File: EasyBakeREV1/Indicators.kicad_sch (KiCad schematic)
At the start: 15 parts, among them U10 STP08CP05

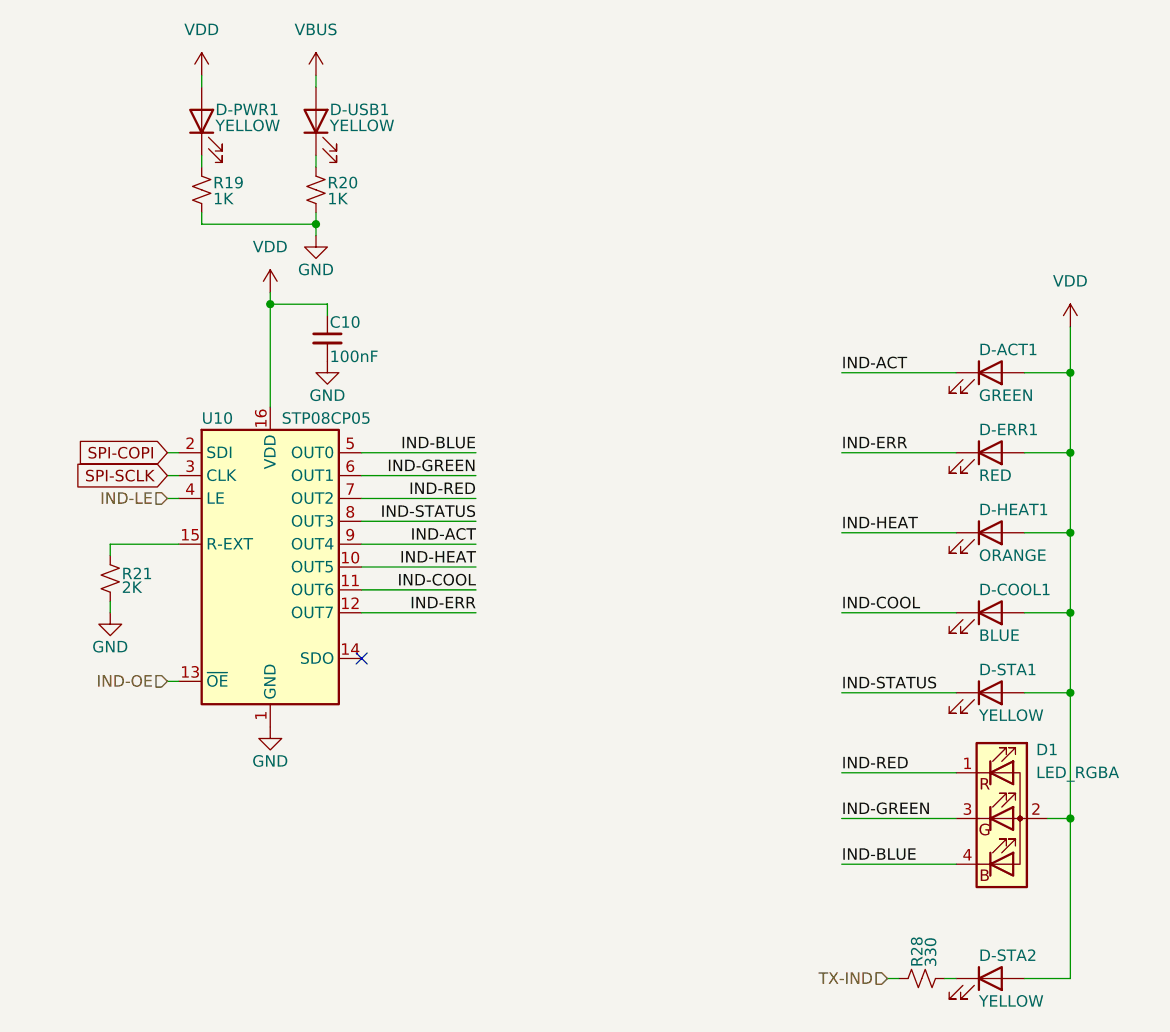
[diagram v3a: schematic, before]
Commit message: Change main pwr to 3.3 due to USB issues
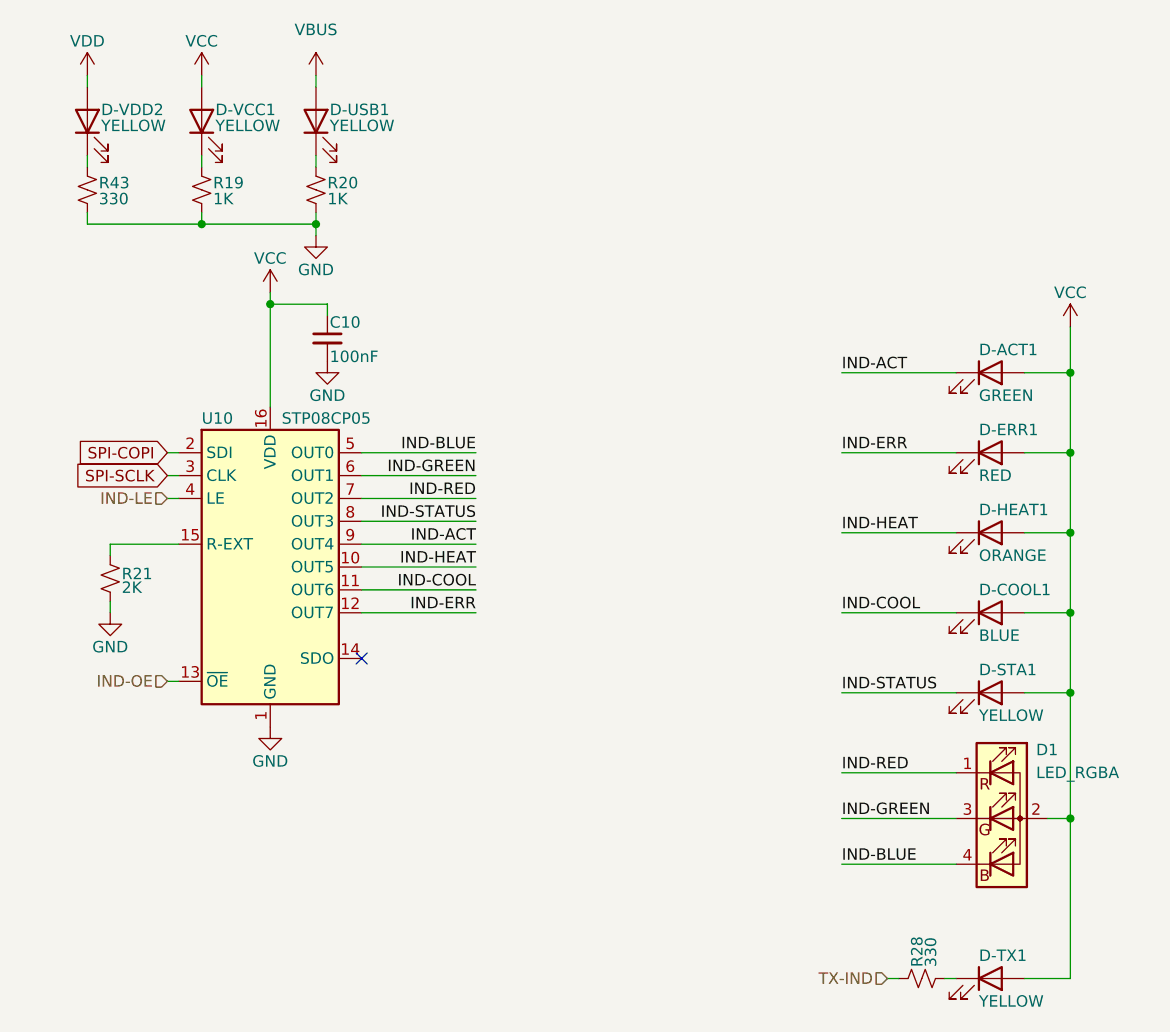
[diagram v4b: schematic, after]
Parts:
- added D-VDD2: YELLOW, LED_SMD:LED_0805_2012Metric_Pad1.15x1.40mm_HandSolder, symbol Device:LED
- added R43: 330, Resistor_SMD:R_0805_2012Metric, symbol Device:R_Small_US
- renumbered D-STA2 to D-TX1, D-PWR1 to D-VCC1
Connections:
- net GND: now also R43.2
- net VDD: now also D-VDD2.2 (A); no longer C10.1, D-ACT1.2 (A), D-COOL1.2 (A), D-ERR1.2 (A), D-HEAT1.2 (A), D-STA1.2 (A), D-TX1.2 (A), D-VCC1.2 (A), D1.2 (GK), U10.16 (VDD)
- new net: D-VDD2.1 (K), R43.1
- new net VCC: C10.1, D-ACT1.2 (A), D-COOL1.2 (A), D-ERR1.2 (A), D-HEAT1.2 (A), D-STA1.2 (A), D-TX1.2 (A), D-VCC1.2 (A), D1.2 (GK), U10.16 (VDD)
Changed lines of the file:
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@@
   (junction (at 45.72 50.8) (diameter 0) (color 0 0 0 0)
+  )
+  (junction (at 38.1 41.91) (diameter 0) (color 0 0 0 0)
   )
   (junction (at 134.62 85.09) (diameter 0) (color 0 0 0 0)
@@
     (stroke (width 0) (type default))
   )
+  (wire (pts (xy 25.4 41.91) (xy 38.1 41.91))
+    (stroke (width 0) (type default))
+  )
   (wire (pts (xy 129.54 67.31) (xy 134.62 67.31))
     (stroke (width 0) (type default))
@@
     (stroke (width 0) (type default))
   )
+  (wire (pts (xy 25.4 40.64) (xy 25.4 41.91))
+    (stroke (width 0) (type default))
+  )
   (wire (pts (xy 109.22 113.03) (xy 121.92 113.03))
     (stroke (width 0) (type default))
@@
     (stroke (width 0) (type default))
   )
+  (wire (pts (xy 25.4 25.4) (xy 25.4 26.67))
+    (stroke (width 0) (type default))
+  )
   (wire (pts (xy 114.3 125.73) (xy 115.57 125.73))
     (stroke (width 0) (type default))
@@
   )
   (wire (pts (xy 34.29 92.71) (xy 35.56 92.71))
+    (stroke (width 0) (type default))
+  )
+  (wire (pts (xy 25.4 34.29) (xy 25.4 35.56))
     (stroke (width 0) (type default))
   )
@@
     )
   )
-  (symbol (lib_id "power:VDD") (at 134.62 53.34 0) (unit 1)
-    (in_bom yes) (on_board yes) (dnp no) (fields_autoplaced)
-    (property "Reference" "#PWR0103" (at 134.62 57.15 0)
-      (effects (font (size 1.27 1.27)) hide)
-    )
-    (property "Value" "VDD" (at 134.62 48.26 0)
-      (effects (font (size 1.27 1.27)))
-    )
-    (property "Footprint" "" (at 134.62 53.34 0)
-      (effects (font (size 1.27 1.27)) hide)
-    )
-    (property "Datasheet" "" (at 134.62 53.34 0)
-      (effects (font (size 1.27 1.27)) hide)
-    )
-    (pin "1")
-    (instances
-      (project "EasyBakeREV1"
-        (path "/e63e39d7-6ac0-4ffd-8aa3-1841a4541b55/a9601474-acad-4e52-ad82-40858ef5b30f"
-          (reference "#PWR0103") (unit 1)
-        )
-      )
-    )
-  )
   (symbol (lib_id "power:GND") (at 50.8 43.18 0) (unit 1)
     (in_bom yes) (on_board yes) (dnp no)
@@
     )
   )
+  (symbol (lib_id "power:VCC") (at 45.72 49.53 0) (unit 1)
+    (in_bom yes) (on_board yes) (dnp no)
+    (property "Reference" "#PWR012" (at 45.72 53.34 0)
+      (effects (font (size 1.27 1.27)) hide)
+    )
+    (property "Value" "VCC" (at 45.72 45.72 0)
+      (effects (font (size 1.27 1.27)))
+    )
+    (property "Footprint" "" (at 45.72 49.53 0)
+      (effects (font (size 1.27 1.27)) hide)
+    )
+    (property "Datasheet" "" (at 45.72 49.53 0)
+      (effects (font (size 1.27 1.27)) hide)
+    )
+    (pin "1")
+    (instances
+      (project "EasyBakeREV1"
+        (path "/e63e39d7-6ac0-4ffd-8aa3-1841a4541b55/a9601474-acad-4e52-ad82-40858ef5b30f"
+          (reference "#PWR012") (unit 1)
+        )
+      )
+    )
+  )
   (symbol (lib_id "Device:LED") (at 38.1 30.48 90) (unit 1)
     (in_bom yes) (on_board yes) (dnp no)
-    (property "Reference" "D-PWR1" (at 39.624 29.21 90)
+    (property "Reference" "D-VCC1" (at 39.624 29.21 90)
       (effects (font (size 1.27 1.27)) (justify right))
     )
@@
       (project "EasyBakeREV1"
         (path "/e63e39d7-6ac0-4ffd-8aa3-1841a4541b55/a9601474-acad-4e52-ad82-40858ef5b30f"
-          (reference "D-PWR1") (unit 1)
+          (reference "D-VCC1") (unit 1)
+        )
+      )
+    )
+  )
+  (symbol (lib_id "power:VCC") (at 134.62 53.34 0) (unit 1)
+    (in_bom yes) (on_board yes) (dnp no)
+    (property "Reference" "#PWR04" (at 134.62 57.15 0)
+      (effects (font (size 1.27 1.27)) hide)
+    )
+    (property "Value" "VCC" (at 134.62 49.53 0)
+      (effects (font (size 1.27 1.27)))
+    )
+    (property "Footprint" "" (at 134.62 53.34 0)
+      (effects (font (size 1.27 1.27)) hide)
+    )
+    (property "Datasheet" "" (at 134.62 53.34 0)
+      (effects (font (size 1.27 1.27)) hide)
+    )
+    (pin "1")
+    (instances
+      (project "EasyBakeREV1"
+        (path "/e63e39d7-6ac0-4ffd-8aa3-1841a4541b55/a9601474-acad-4e52-ad82-40858ef5b30f"
+          (reference "#PWR04") (unit 1)
         )
       )
@@
     )
   )
+  (symbol (lib_id "Device:LED") (at 25.4 30.48 90) (unit 1)
+    (in_bom yes) (on_board yes) (dnp no)
+    (property "Reference" "D-VDD2" (at 26.924 29.21 90)
+      (effects (font (size 1.27 1.27)) (justify right))
+    )
+    (property "Value" "YELLOW" (at 26.924 30.988 90)
+      (effects (font (size 1.27 1.27)) (justify right))
+    )
+    (property "Footprint" "LED_SMD:LED_0805_2012Metric_Pad1.15x1.40mm_HandSolder" (at 25.4 30.48 0)
+      (effects (font (size 1.27 1.27)) hide)
+    )
+    (property "Datasheet" "~" (at 25.4 30.48 0)
+      (effects (font (size 1.27 1.27)) hide)
+    )
+    (pin "1")
+    (pin "2")
+    (instances
+      (project "EasyBakeREV1"
+        (path "/e63e39d7-6ac0-4ffd-8aa3-1841a4541b55/a9601474-acad-4e52-ad82-40858ef5b30f"
+          (reference "D-VDD2") (unit 1)
+        )
+      )
+    )
+  )
   (symbol (lib_id "Device:LED") (at 50.8 30.48 90) (unit 1)
     (in_bom yes) (on_board yes) (dnp no)
@@
   (symbol (lib_id "Device:LED") (at 125.73 125.73 0) (unit 1)
     (in_bom yes) (on_board yes) (dnp no)
-    (property "Reference" "D-STA2" (at 124.46 123.19 0)
+    (property "Reference" "D-TX1" (at 124.46 123.19 0)
       (effects (font (size 1.27 1.27)) (justify left))
     )
@@
       (project "EasyBakeREV1"
         (path "/e63e39d7-6ac0-4ffd-8aa3-1841a4541b55/a9601474-acad-4e52-ad82-40858ef5b30f"
-          (reference "D-STA2") (unit 1)
+          (reference "D-TX1") (unit 1)
         )
       )
@@
     )
   )
-  (symbol (lib_id "power:VDD") (at 45.72 49.53 0) (unit 1)
-    (in_bom yes) (on_board yes) (dnp no) (fields_autoplaced)
-    (property "Reference" "#PWR0105" (at 45.72 53.34 0)
-      (effects (font (size 1.27 1.27)) hide)
-    )
-    (property "Value" "VDD" (at 45.72 44.45 0)
-      (effects (font (size 1.27 1.27)))
-    )
-    (property "Footprint" "" (at 45.72 49.53 0)
-      (effects (font (size 1.27 1.27)) hide)
-    )
-    (property "Datasheet" "" (at 45.72 49.53 0)
-      (effects (font (size 1.27 1.27)) hide)
-    )
-    (pin "1")
-    (instances
-      (project "EasyBakeREV1"
-        (path "/e63e39d7-6ac0-4ffd-8aa3-1841a4541b55/a9601474-acad-4e52-ad82-40858ef5b30f"
-          (reference "#PWR0105") (unit 1)
+  (symbol (lib_id "power:VCC") (at 38.1 25.4 0) (unit 1)
+    (in_bom yes) (on_board yes) (dnp no)
+    (property "Reference" "#PWR020" (at 38.1 29.21 0)
+      (effects (font (size 1.27 1.27)) hide)
+    )
+    (property "Value" "VCC" (at 38.1 21.59 0)
+      (effects (font (size 1.27 1.27)))
+    )
+    (property "Footprint" "" (at 38.1 25.4 0)
+      (effects (font (size 1.27 1.27)) hide)
+    )
+    (property "Datasheet" "" (at 38.1 25.4 0)
+      (effects (font (size 1.27 1.27)) hide)
+    )
+    (pin "1")
+    (instances
+      (project "EasyBakeREV1"
+        (path "/e63e39d7-6ac0-4ffd-8aa3-1841a4541b55/a9601474-acad-4e52-ad82-40858ef5b30f"
+          (reference "#PWR020") (unit 1)
+        )
+      )
+    )
+  )
+  (symbol (lib_id "power:VDD") (at 25.4 25.4 0) (unit 1)
+    (in_bom yes) (on_board yes) (dnp no)
+    (property "Reference" "#PWR025" (at 25.4 29.21 0)
+      (effects (font (size 1.27 1.27)) hide)
+    )
+    (property "Value" "VDD" (at 25.4 21.59 0)
+      (effects (font (size 1.27 1.27)))
+    )
+    (property "Footprint" "" (at 25.4 25.4 0)
+      (effects (font (size 1.27 1.27)) hide)
+    )
+    (property "Datasheet" "" (at 25.4 25.4 0)
+      (effects (font (size 1.27 1.27)) hide)
+    )
+    (pin "1")
+    (instances
+      (project "EasyBakeREV1"
+        (path "/e63e39d7-6ac0-4ffd-8aa3-1841a4541b55/a9601474-acad-4e52-ad82-40858ef5b30f"
+          (reference "#PWR025") (unit 1)
         )
       )
@@
     )
   )
-  (symbol (lib_id "power:VDD") (at 38.1 25.4 0) (unit 1)
-    (in_bom yes) (on_board yes) (dnp no) (fields_autoplaced)
-    (property "Reference" "#PWR054" (at 38.1 29.21 0)
-      (effects (font (size 1.27 1.27)) hide)
-    )
-    (property "Value" "VDD" (at 38.1 20.32 0)
-      (effects (font (size 1.27 1.27)))
-    )
-    (property "Footprint" "" (at 38.1 25.4 0)
-      (effects (font (size 1.27 1.27)) hide)
-    )
-    (property "Datasheet" "" (at 38.1 25.4 0)
-      (effects (font (size 1.27 1.27)) hide)
-    )
-    (pin "1")
-    (instances
-      (project "EasyBakeREV1"
-        (path "/e63e39d7-6ac0-4ffd-8aa3-1841a4541b55/a9601474-acad-4e52-ad82-40858ef5b30f"
-          (reference "#PWR054") (unit 1)
-        )
-      )
-    )
-  )
   (symbol (lib_id "Device:LED") (at 125.73 76.2 0) (unit 1)
     (in_bom yes) (on_board yes) (dnp no)
@@
         )
       )
+    )
+  )
+  (symbol (lib_id "Device:R_Small_US") (at 25.4 38.1 0) (unit 1)
+    (in_bom yes) (on_board yes) (dnp no)
+    (property "Reference" "R43" (at 26.67 37.338 0)
+      (effects (font (size 1.27 1.27)) (justify left))
+    )
+    (property "Value" "330" (at 26.67 39.116 0)
+      (effects (font (size 1.27 1.27)) (justify left))
+    )
+    (property "Footprint" "Resistor_SMD:R_0805_2012Metric" (at 25.4 38.1 0)
+      (effects (font (size 1.27 1.27)) hide)
+    )
+    (property "Datasheet" "~" (at 25.4 38.1 0)
+      (effects (font (size 1.27 1.27)) hide)
+    )
+    (property "Schematic" "" (at 25.4 38.1 0)
+      (effects (font (size 1.27 1.27)) hide)
+    )
+    (property "PartNumber" "" (at 25.4 38.1 0)
+      (effects (font (size 1.27 1.27)))
+    )
+    (property "SupplierPN" "" (at 25.4 38.1 0)
+      (effects (font (size 1.27 1.27)) hide)
+    )
+    (pin "1")
+    (pin "2")
+    (instances
+      (project "EasyBakeREV1"
+        (path "/e63e39d7-6ac0-4ffd-8aa3-1841a4541b55/a9601474-acad-4e52-ad82-40858ef5b30f"
+          (reference "R43") (unit 1)
+        )
+      )

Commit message: Replaced MCU - started layout
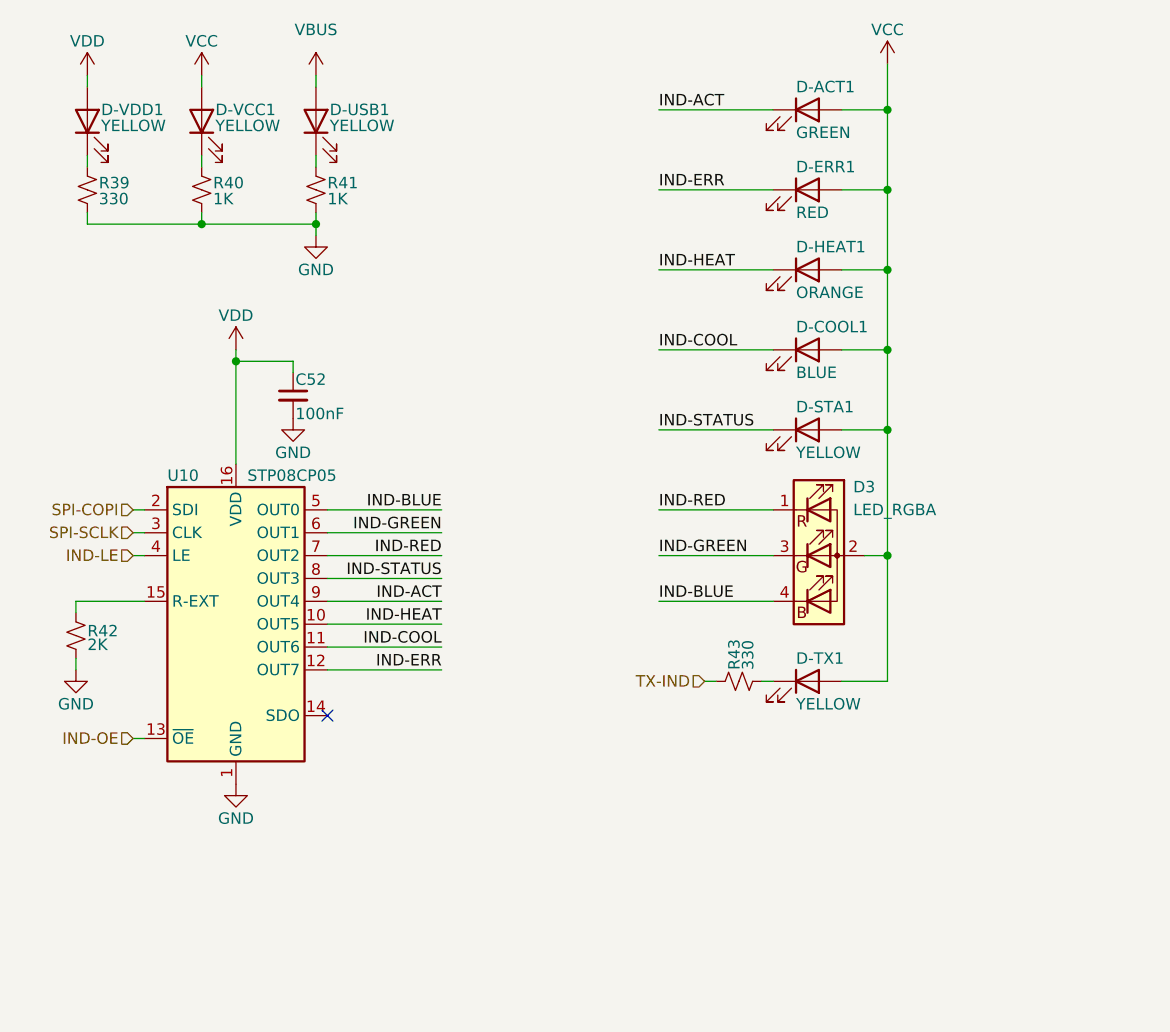
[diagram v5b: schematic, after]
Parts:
- R39: renamed from R43; footprint Resistor_SMD:R_0805_2012Metric -> Resistor_SMD:R_0603_1608Metric
- R40: renamed from R19; footprint Resistor_SMD:R_0805_2012Metric -> Resistor_SMD:R_0603_1608Metric
- R41: renamed from R20; footprint Resistor_SMD:R_0805_2012Metric -> Resistor_SMD:R_0603_1608Metric
- R42: renamed from R21; footprint Resistor_SMD:R_0805_2012Metric -> Resistor_SMD:R_0402_1005Metric
- renumbered C10 to C52, D-VDD2 to D-VDD1, D1 to D3, R28 to R43
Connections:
- net VCC: no longer C52.1, U10.16 (VDD)
- net VDD: now also C52.1, U10.16 (VDD)
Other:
- moved on the sheet: C52, D-ACT1, D-COOL1, D-ERR1, D-HEAT1, D-STA1, D-TX1, D3, R42, R43, U10

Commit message: Rearrange footprints and start layout
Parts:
- U10: footprint Package_SO:TSSOP-16-1EP_4.4x5mm_P0.65mm_EP3x3mm -> Package_SO:TSSOP-16_4.4x5mm_P0.65mm
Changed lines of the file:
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@@
       (effects (font (size 1.27 1.27)) (justify left))
     )
-    (property "Footprint" "Package_SO:TSSOP-16-1EP_4.4x5mm_P0.65mm_EP3x3mm" (at 41.91 86.36 0)
+    (property "Footprint" "Package_SO:TSSOP-16_4.4x5mm_P0.65mm" (at 41.91 86.36 0)
       (effects (font (size 1.27 1.27)) hide)
     )
@@
       (effects (font (size 1.27 1.27)) hide)
     )
+    (property "Schematic" "" (at 41.91 86.36 0)
+      (effects (font (size 1.27 1.27)) hide)
+    )
+    (property "PartNumber" "" (at 41.91 86.36 0)
+      (effects (font (size 1.27 1.27)))
+    )
+    (property "SupplierPN" "" (at 41.91 86.36 0)
+      (effects (font (size 1.27 1.27)) hide)
+    )
